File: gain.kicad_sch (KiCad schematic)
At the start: 5 parts, among them U7 TL072

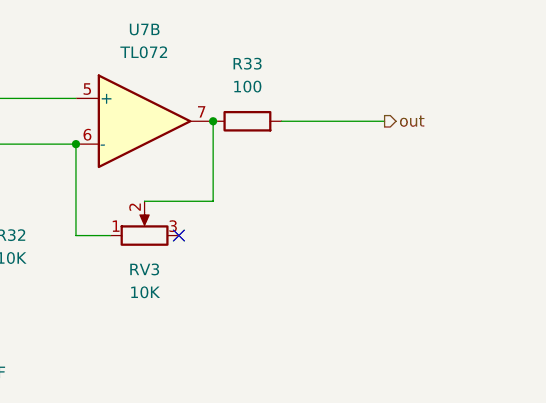
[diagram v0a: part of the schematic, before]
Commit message: Fix output filters
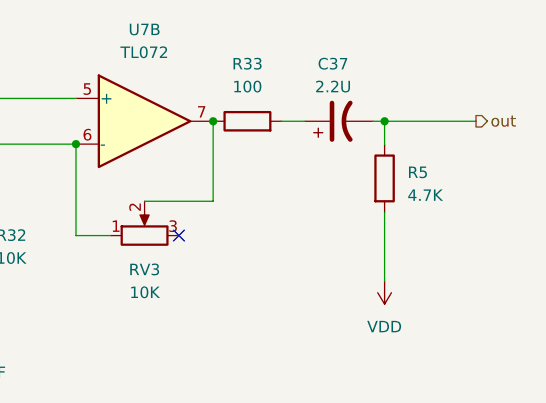
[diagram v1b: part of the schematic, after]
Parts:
- added C37: 2.2U, symbol Device:C_Polarized_US
- added R5: 4.7K, symbol Device:R
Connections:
- net out: now also C37.2, R5.1; no longer R33.2
- new net: C37.1, R33.2
- new net VDD: R5.2
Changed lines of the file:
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@@
   (junction (at 101.6 71.12) (diameter 0) (color 0 0 0 0)
   )
+  (junction (at 135.89 68.58) (diameter 0) (color 0 0 0 0)
+  )
   (no_connect (at 113.03 81.28))
-  (wire (pts (xy 90.17 86.36) (xy 90.17 91.44))
+  (wire (pts (xy 135.89 68.58) (xy 135.89 71.12))
     (stroke (width 0) (type default))
   )
-  (wire (pts (xy 124.46 68.58) (xy 135.89 68.58))
+  (wire (pts (xy 90.17 86.36) (xy 90.17 91.44))
     (stroke (width 0) (type default))
   )
@@
   )
   (wire (pts (xy 90.17 78.74) (xy 90.17 71.12))
+    (stroke (width 0) (type default))
+  )
+  (wire (pts (xy 134.62 68.58) (xy 135.89 68.58))
+    (stroke (width 0) (type default))
+  )
+  (wire (pts (xy 135.89 68.58) (xy 146.05 68.58))
     (stroke (width 0) (type default))
   )
@@
     (stroke (width 0) (type default))
   )
+  (wire (pts (xy 135.89 78.74) (xy 135.89 86.36))
+    (stroke (width 0) (type default))
+  )
   (wire (pts (xy 101.6 81.28) (xy 101.6 71.12))
     (stroke (width 0) (type default))
@@
     (stroke (width 0) (type default))
   )
+  (wire (pts (xy 124.46 68.58) (xy 127 68.58))
+    (stroke (width 0) (type default))
+  )
   (hierarchical_label "in" (shape input) (at 63.5 66.04 180) (fields_autoplaced)
     (effects (font (size 1.27 1.27)) (justify right))
   )
-  (hierarchical_label "out" (shape output) (at 135.89 68.58 0) (fields_autoplaced)
+  (hierarchical_label "out" (shape output) (at 146.05 68.58 0) (fields_autoplaced)
     (effects (font (size 1.27 1.27)) (justify left))
+  )
+  (symbol (lib_id "power:VDD") (at 135.89 86.36 180) (unit 1)
+    (in_bom yes) (on_board yes) (dnp no) (fields_autoplaced)
+    (property "Reference" "#PWR035" (at 135.89 82.55 0)
+      (effects (font (size 1.27 1.27)) hide)
+    )
+    (property "Value" "VDD" (at 135.89 91.44 0)
+      (effects (font (size 1.27 1.27)))
+    )
+    (property "Footprint" "" (at 135.89 86.36 0)
+      (effects (font (size 1.27 1.27)) hide)
+    )
+    (property "Datasheet" "" (at 135.89 86.36 0)
+      (effects (font (size 1.27 1.27)) hide)
+    )
+    (pin "1")
+    (instances
+      (project "crossover"
+        (path "/3c8df2a5-e9f9-4495-af40-aa221f0b3fa5/28472e3b-9819-48c0-b63f-39bc09c5cac5"
+          (reference "#PWR035") (unit 1)
+        )
+        (path "/3c8df2a5-e9f9-4495-af40-aa221f0b3fa5/26fb0579-508e-4f39-8fcc-d72882569c12"
+          (reference "#PWR04") (unit 1)
+        )
+        (path "/3c8df2a5-e9f9-4495-af40-aa221f0b3fa5/8c997b3b-7bf2-44b2-ab14-da860701b424"
+          (reference "#PWR05") (unit 1)
+        )
+      )
+    )
   )
   (symbol (lib_id "Amplifier_Operational:TL072") (at 109.22 68.58 0) (unit 2)
@@
         )
       )
+    )
+  )
+  (symbol (lib_id "Device:R") (at 135.89 74.93 0) (unit 1)
+    (in_bom yes) (on_board yes) (dnp no) (fields_autoplaced)
+    (property "Reference" "R5" (at 138.43 74.295 0)
+      (effects (font (size 1.27 1.27)) (justify left))
+    )
+    (property "Value" "4.7K" (at 138.43 76.835 0)
+      (effects (font (size 1.27 1.27)) (justify left))
+    )
+    (property "Footprint" "" (at 134.112 74.93 90)
+      (effects (font (size 1.27 1.27)) hide)
+    )
+    (property "Datasheet" "~" (at 135.89 74.93 0)
+      (effects (font (size 1.27 1.27)) hide)
+    )
+    (pin "1")
+    (pin "2")
+    (instances
+      (project "crossover"
+        (path "/3c8df2a5-e9f9-4495-af40-aa221f0b3fa5/28472e3b-9819-48c0-b63f-39bc09c5cac5"
+          (reference "R5") (unit 1)
+        )
+        (path "/3c8df2a5-e9f9-4495-af40-aa221f0b3fa5/26fb0579-508e-4f39-8fcc-d72882569c12"
+          (reference "R3") (unit 1)
+        )
+        (path "/3c8df2a5-e9f9-4495-af40-aa221f0b3fa5/8c997b3b-7bf2-44b2-ab14-da860701b424"
+          (reference "R4") (unit 1)
+        )
+      )
+    )
+  )
+  (symbol (lib_id "Device:C_Polarized_US") (at 130.81 68.58 90) (unit 1)
+    (in_bom yes) (on_board yes) (dnp no) (fields_autoplaced)
+    (property "Reference" "C37" (at 130.175 62.23 90)
+      (effects (font (size 1.27 1.27)))
+    )
+    (property "Value" "2.2U" (at 130.175 64.77 90)
+      (effects (font (size 1.27 1.27)))
+    )
+    (property "Footprint" "" (at 130.81 68.58 0)
+      (effects (font (size 1.27 1.27)) hide)
+    )
+    (property "Datasheet" "~" (at 130.81 68.58 0)
+      (effects (font (size 1.27 1.27)) hide)
+    )
+    (pin "1")
+    (pin "2")
+    (instances
+      (project "crossover"
+        (path "/3c8df2a5-e9f9-4495-af40-aa221f0b3fa5/28472e3b-9819-48c0-b63f-39bc09c5cac5"
+          (reference "C37") (unit 1)
+        )
+        (path "/3c8df2a5-e9f9-4495-af40-aa221f0b3fa5/26fb0579-508e-4f39-8fcc-d72882569c12"
+          (reference "C28") (unit 1)
+        )
+        (path "/3c8df2a5-e9f9-4495-af40-aa221f0b3fa5/8c997b3b-7bf2-44b2-ab14-da860701b424"
+          (reference "C29") (unit 1)
+        )
+      )

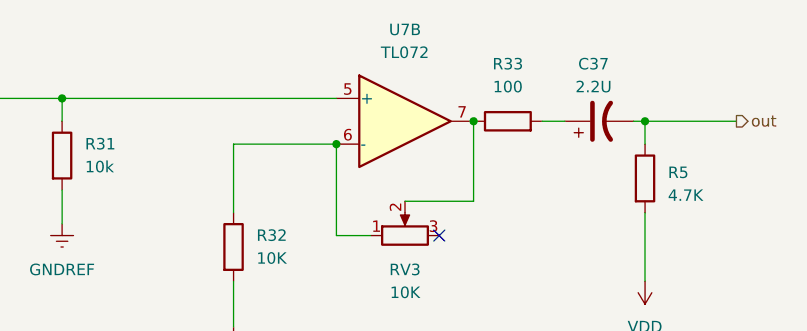
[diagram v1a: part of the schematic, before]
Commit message: Allow stereo/mono switching for Sub
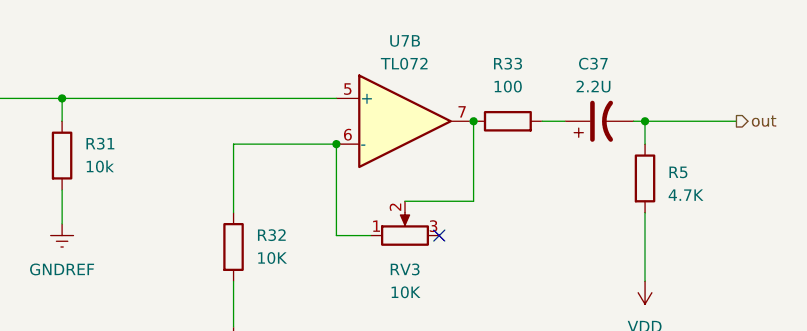
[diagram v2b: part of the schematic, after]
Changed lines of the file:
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@@
           (reference "#PWR05") (unit 1)
         )
+        (path "/3c8df2a5-e9f9-4495-af40-aa221f0b3fa5/6a6e002a-0565-47d4-a8fe-a1e284818334"
+          (reference "#PWR04") (unit 1)
+        )
       )
     )
@@
   (symbol (lib_id "Amplifier_Operational:TL072") (at 109.22 68.58 0) (unit 2)
     (in_bom yes) (on_board yes) (dnp no) (fields_autoplaced)
-    (property "Reference" "U7" (at 109.22 58.42 0)
-      (effects (font (size 1.27 1.27)))
-    )
-    (property "Value" "TL072" (at 109.22 60.96 0)
+    (property "Reference" "U7" (at 109.22 59.69 0)
+      (effects (font (size 1.27 1.27)))
+    )
+    (property "Value" "TL072" (at 109.22 62.23 0)
       (effects (font (size 1.27 1.27)))
     )
@@
           (reference "U6") (unit 1)
         )
+        (path "/3c8df2a5-e9f9-4495-af40-aa221f0b3fa5/6a6e002a-0565-47d4-a8fe-a1e284818334"
+          (reference "U6") (unit 2)
+        )
       )
     )
@@
           (reference "R4") (unit 1)
         )
+        (path "/3c8df2a5-e9f9-4495-af40-aa221f0b3fa5/6a6e002a-0565-47d4-a8fe-a1e284818334"
+          (reference "R3") (unit 1)
+        )
       )
     )
@@
           (reference "C29") (unit 1)
         )
+        (path "/3c8df2a5-e9f9-4495-af40-aa221f0b3fa5/6a6e002a-0565-47d4-a8fe-a1e284818334"
+          (reference "C28") (unit 1)
+        )
       )
     )
@@
           (reference "RV1") (unit 1)
         )
+        (path "/3c8df2a5-e9f9-4495-af40-aa221f0b3fa5/6a6e002a-0565-47d4-a8fe-a1e284818334"
+          (reference "RV1") (unit 1)
+        )
       )
     )
@@
           (reference "R23") (unit 1)
         )
+        (path "/3c8df2a5-e9f9-4495-af40-aa221f0b3fa5/6a6e002a-0565-47d4-a8fe-a1e284818334"
+          (reference "R23") (unit 1)
+        )
       )
     )
@@
           (reference "#PWR014") (unit 1)
         )
+        (path "/3c8df2a5-e9f9-4495-af40-aa221f0b3fa5/6a6e002a-0565-47d4-a8fe-a1e284818334"
+          (reference "#PWR014") (unit 1)
+        )
       )
     )
@@
           (reference "#PWR015") (unit 1)
         )
+        (path "/3c8df2a5-e9f9-4495-af40-aa221f0b3fa5/6a6e002a-0565-47d4-a8fe-a1e284818334"
+          (reference "#PWR015") (unit 1)
+        )
       )
     )
@@
           (reference "R24") (unit 1)
         )
+        (path "/3c8df2a5-e9f9-4495-af40-aa221f0b3fa5/6a6e002a-0565-47d4-a8fe-a1e284818334"
+          (reference "R24") (unit 1)
+        )
       )
     )
@@
           (reference "R27") (unit 1)
         )
+        (path "/3c8df2a5-e9f9-4495-af40-aa221f0b3fa5/6a6e002a-0565-47d4-a8fe-a1e284818334"
+          (reference "R27") (unit 1)
+        )

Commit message: Re-annotate and run erc
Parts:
- renumbered C37 to C34, R31 to R38, R32 to R39, R33 to R40, R5 to R41

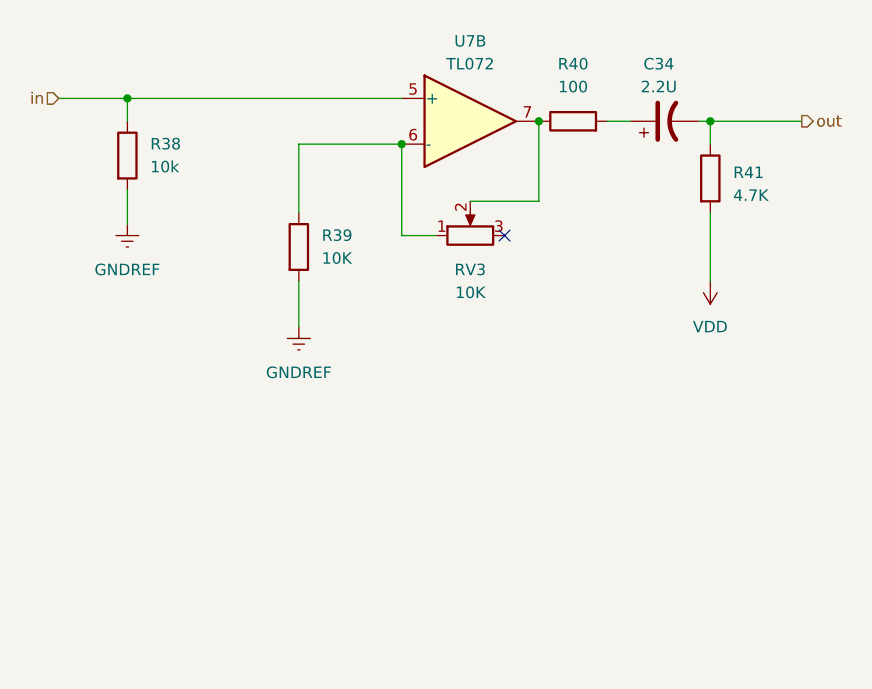
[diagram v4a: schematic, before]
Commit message: Switch to TL074
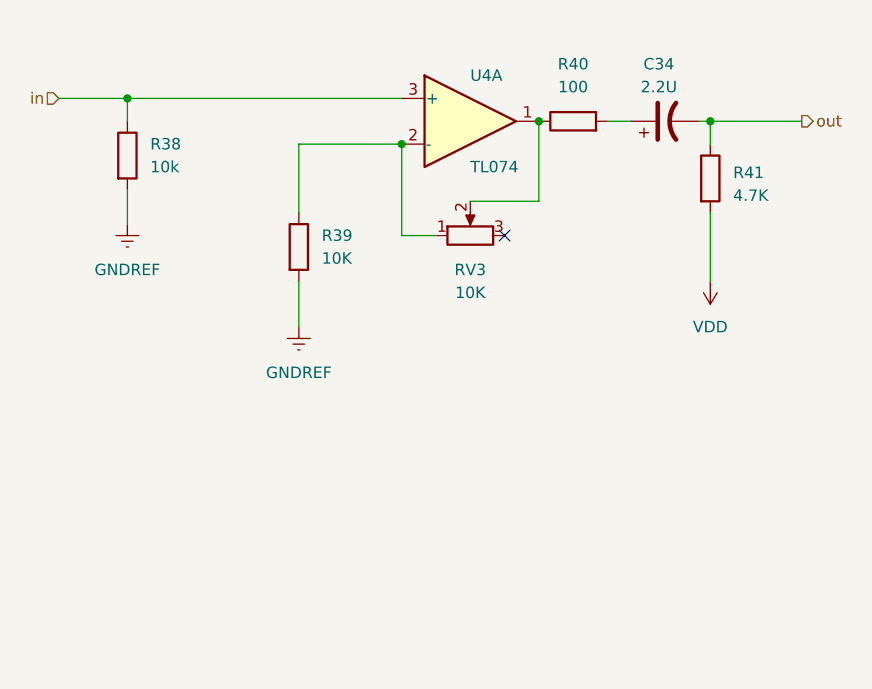
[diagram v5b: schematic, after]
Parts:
- U4: renamed from U7; value TL072 -> TL074; footprint Package_DIP:DIP-8_W7.62mm_Socket -> (none); symbol Amplifier_Operational:TL072 -> Amplifier_Operational:TL074
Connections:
- net in: now also U4.3 (+); no longer U4.5 (+)
- net at R39.1, RV3.1: now also U4.2 (-); no longer U4.6 (-)
- net at R40.1, RV3.2: now also U4.1; no longer U4.7
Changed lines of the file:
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@@
     )
   )
-  (symbol (lib_id "Amplifier_Operational:TL072") (at 109.22 68.58 0) (unit 2)
+  (symbol (lib_id "Amplifier_Operational:TL074") (at 109.22 68.58 0) (unit 1)
     (in_bom yes) (on_board yes) (dnp no) (fields_autoplaced)
-    (property "Reference" "U7" (at 109.22 59.69 0)
-      (effects (font (size 1.27 1.27)))
+    (property "Reference" "U4" (at 109.22 63.5 0)
+      (effects (font (size 1.27 1.27)) (justify left))
     )
-    (property "Value" "TL072" (at 109.22 62.23 0)
-      (effects (font (size 1.27 1.27)))
+    (property "Value" "TL074" (at 109.22 73.66 0)
+      (effects (font (size 1.27 1.27)) (justify left))
     )
-    (property "Footprint" "Package_DIP:DIP-8_W7.62mm_Socket" (at 109.22 68.58 0)
+    (property "Footprint" "" (at 107.95 66.04 0)
       (effects (font (size 1.27 1.27)) hide)
     )
-    (property "Datasheet" "http://www.ti.com/lit/ds/symlink/tl071.pdf" (at 109.22 68.58 0)
+    (property "Datasheet" "http://www.ti.com/lit/ds/symlink/tl071.pdf" (at 110.49 63.5 0)
       (effects (font (size 1.27 1.27)) hide)
     )
@@
     (pin "6")
     (pin "7")
+    (pin "10")
+    (pin "8")
+    (pin "9")
+    (pin "12")
+    (pin "13")
+    (pin "14")
+    (pin "11")
     (pin "4")
-    (pin "8")
     (instances
       (project "crossover"
         (path "/3c8df2a5-e9f9-4495-af40-aa221f0b3fa5/28472e3b-9819-48c0-b63f-39bc09c5cac5"
-          (reference "U7") (unit 2)
+          (reference "U4") (unit 1)
         )
         (path "/3c8df2a5-e9f9-4495-af40-aa221f0b3fa5/8c997b3b-7bf2-44b2-ab14-da860701b424"
-          (reference "U7") (unit 1)
+          (reference "U4") (unit 2)
         )
         (path "/3c8df2a5-e9f9-4495-af40-aa221f0b3fa5/26fb0579-508e-4f39-8fcc-d72882569c12"
-          (reference "U6") (unit 1)
+          (reference "U4") (unit 3)
         )
         (path "/3c8df2a5-e9f9-4495-af40-aa221f0b3fa5/6a6e002a-0565-47d4-a8fe-a1e284818334"
-          (reference "U6") (unit 2)
+          (reference "U4") (unit 4)
         )
       )

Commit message: Assign footprints to everything
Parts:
- C34: footprint (none) -> Capacitor_THT:CP_Radial_D5.0mm_P2.50mm
- R38, R39: footprint Resistor_THT:R_Axial_DIN0207_L6.3mm_D2.5mm_P7.62mm_Horizontal -> Resistor_SMD:R_1206_3216Metric_Pad1.30x1.75mm_HandSolder
- R41: footprint (none) -> Resistor_SMD:R_1210_3225Metric_Pad1.30x2.65mm_HandSolder
- U4: footprint (none) -> Package_SO:SOIC-14_3.9x8.7mm_P1.27mm
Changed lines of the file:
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@@
       (effects (font (size 1.27 1.27)) (justify left))
     )
-    (property "Footprint" "" (at 107.95 66.04 0)
+    (property "Footprint" "Package_SO:SOIC-14_3.9x8.7mm_P1.27mm" (at 107.95 66.04 0)
       (effects (font (size 1.27 1.27)) hide)
     )
@@
       (effects (font (size 1.27 1.27)) (justify left))
     )
-    (property "Footprint" "" (at 134.112 74.93 90)
+    (property "Footprint" "Resistor_SMD:R_1210_3225Metric_Pad1.30x2.65mm_HandSolder" (at 134.112 74.93 90)
       (effects (font (size 1.27 1.27)) hide)
     )
@@
       (effects (font (size 1.27 1.27)))
     )
-    (property "Footprint" "" (at 130.81 68.58 0)
+    (property "Footprint" "Capacitor_THT:CP_Radial_D5.0mm_P2.50mm" (at 130.81 68.58 0)
       (effects (font (size 1.27 1.27)) hide)
     )
@@
       (effects (font (size 1.27 1.27)) (justify left))
     )
-    (property "Footprint" "Resistor_THT:R_Axial_DIN0207_L6.3mm_D2.5mm_P7.62mm_Horizontal" (at 69.342 72.39 90)
+    (property "Footprint" "Resistor_SMD:R_1206_3216Metric_Pad1.30x1.75mm_HandSolder" (at 69.342 72.39 90)
       (effects (font (size 1.27 1.27)) hide)
     )
@@
       (effects (font (size 1.27 1.27)) (justify left))
     )
-    (property "Footprint" "Resistor_THT:R_Axial_DIN0207_L6.3mm_D2.5mm_P7.62mm_Horizontal" (at 88.392 82.55 90)
-      (effects (font (size 1.27 1.27)) hide)
-    )
+    (property "Footprint" "Resistor_SMD:R_1206_3216Metric_Pad1.30x1.75mm_HandSolder" (at 88.392 82.55 90)
+      (effects (font (size 1.27 1.27)) hide)
+    )
